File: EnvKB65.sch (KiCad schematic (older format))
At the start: 153 parts, among them U1 Pico

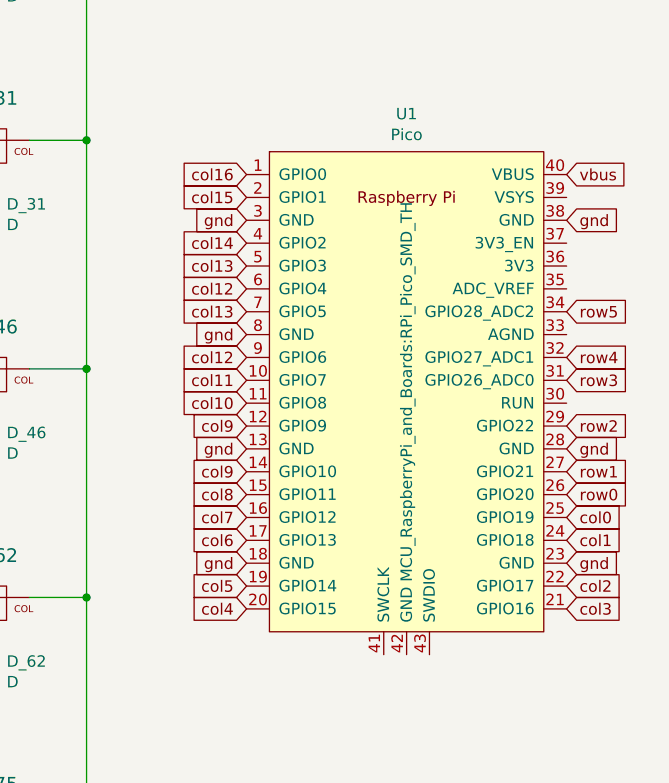
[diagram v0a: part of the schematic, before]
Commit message: slimmed design down a bit at the cost of some keys
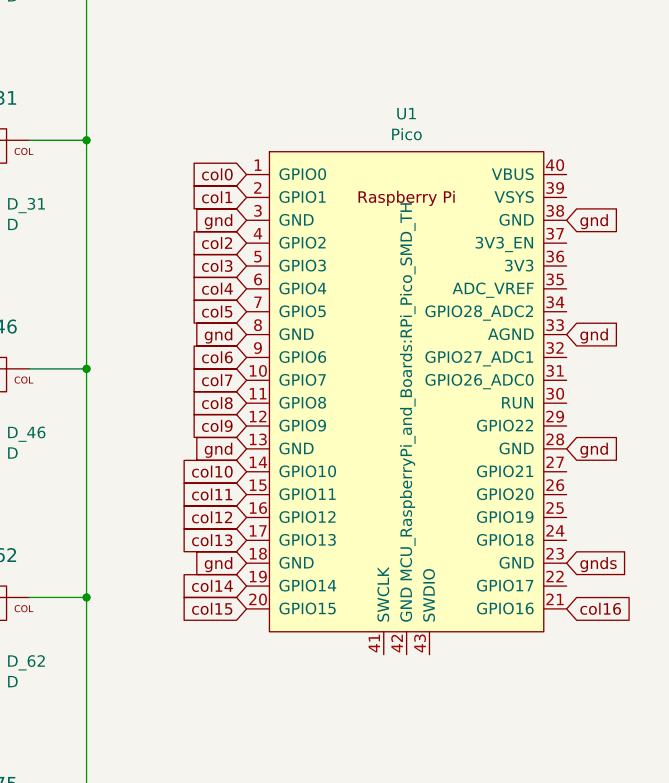
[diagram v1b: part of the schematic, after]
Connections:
- net col0: now also U1.1 (GPIO0); no longer U1.25 (GPIO19)
- net col1: now also U1.2 (GPIO1); no longer U1.24 (GPIO18)
- net col10: now also U1.14 (GPIO10); no longer U1.11 (GPIO8)
- net col11: now also U1.15 (GPIO11); no longer U1.10 (GPIO7)
- net col12: now also U1.16 (GPIO12); no longer U1.6 (GPIO4), U1.9 (GPIO6)
- net col13: now also U1.17 (GPIO13); no longer U1.5 (GPIO3), U1.7 (GPIO5)
- net col14: now also U1.19 (GPIO14); no longer U1.4 (GPIO2)
- net col15: now also U1.20 (GPIO15); no longer U1.2 (GPIO1)
- net col16: now also U1.21 (GPIO16); no longer U1.1 (GPIO0)
- net col2: now also U1.4 (GPIO2); no longer U1.22 (GPIO17)
- net col3: now also U1.5 (GPIO3); no longer U1.21 (GPIO16)
- net col4: now also U1.6 (GPIO4); no longer U1.20 (GPIO15)
- net col5: now also U1.7 (GPIO5); no longer U1.19 (GPIO14)
- net col6: now also U1.9 (GPIO6); no longer U1.17 (GPIO13)
- net col7: now also U1.10 (GPIO7); no longer U1.16 (GPIO12)
- net col8: now also U1.11 (GPIO8); no longer U1.15 (GPIO11)
- net col9: no longer U1.14 (GPIO10)
- net gnd: now also U1.33 (AGND); no longer U1.23 (GND)
- net row0: no longer U1.26 (GPIO20)
- net row1: no longer U1.27 (GPIO21)
- net row2: no longer U1.29 (GPIO22)
- net row3: no longer U1.31 (GPIO26_ADC0)
- net row4: no longer U1.32 (GPIO27_ADC1)
- net row5: no longer names the net of U1.34 (GPIO28_ADC2)
- net vbus: no longer names the net of U1.40 (VBUS)
- new net gnds: U1.23 (GND)
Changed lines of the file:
@@
 Wire Wire Line
 	17800 650  17800 950
-$Comp
-L MX_Alps_Hybrid:MX-NoLED K_15
-U 1 1 00000151
-P 17400 1000
-F 0 "K_15" H 17400 1233 60  0000 C CNN
-F 1 "KEYSW" H 17400 900 60  0001 C CNN
-F 2 "MX_Only:MXOnly-1U-NoLED" H 17400 1000 60  0001 C CNN
-F 3 "" H 17400 1000 60  0000 C CNN
-	1    17400 1000
-	1    0    0    -1
-$EndComp
-$Comp
-L Device:D_Small D_15
-U 1 1 00000150
-P 17350 1300
-F 0 "D_15" V 17420 1200 50  0000 R CNN
-F 1 "D" V 17330 1200 50  0000 R CNN
-F 2 "Diode_SMD:D_SOD-123" H 17050 1250 50  0001 C CNN
-F 3 "~" H 17050 1250 50  0001 C CNN
-	1    17350 1300
-	0    -1   -1   0
-$EndComp
 Wire Wire Line
 	17550 950  17800 950
-Wire Wire Line
-	17350 1150 17350 1200
 Connection ~ 17800 950
 Text GLabel 900  2400 0    50   Input ~ 0
@@
 Connection ~ 16800 1950
 Connection ~ 16350 2400
-$Comp
-L MX_Alps_Hybrid:MX-NoLED K_31
-U 1 1 00000311
-P 17400 2000
-F 0 "K_31" H 17400 2233 60  0000 C CNN
-F 1 "KEYSW" H 17400 1900 60  0001 C CNN
-F 2 "MX_Only:MXOnly-1U-NoLED" H 17400 2000 60  0001 C CNN
-F 3 "" H 17400 2000 60  0000 C CNN
-	1    17400 2000
-	1    0    0    -1
-$EndComp
-$Comp
-L Device:D_Small D_31
-U 1 1 00000310
-P 17350 2300
-F 0 "D_31" V 17420 2200 50  0000 R CNN
-F 1 "D" V 17330 2200 50  0000 R CNN
-F 2 "Diode_SMD:D_SOD-123" H 17050 2250 50  0001 C CNN
-F 3 "~" H 17050 2250 50  0001 C CNN
-	1    17350 2300
-	0    -1   -1   0
-$EndComp
 Wire Wire Line
 	17550 1950 17800 1950
-Wire Wire Line
-	17350 2150 17350 2200
 Connection ~ 17800 1950
 Text GLabel 900  3400 0    50   Input ~ 0
@@
 Connection ~ 16800 2950
 Connection ~ 16350 3400
-$Comp
-L MX_Alps_Hybrid:MX-NoLED K_46
-U 1 1 00000461
-P 17400 3000
-F 0 "K_46" H 17400 3233 60  0000 C CNN
-F 1 "KEYSW" H 17400 2900 60  0001 C CNN
-F 2 "MX_Only:MXOnly-1U-NoLED" H 17400 3000 60  0001 C CNN
-F 3 "" H 17400 3000 60  0000 C CNN
-	1    17400 3000
-	1    0    0    -1
-$EndComp
-$Comp
-L Device:D_Small D_46
-U 1 1 00000460
-P 17350 3300
-F 0 "D_46" V 17420 3200 50  0000 R CNN
-F 1 "D" V 17330 3200 50  0000 R CNN
-F 2 "Diode_SMD:D_SOD-123" H 17050 3250 50  0001 C CNN
-F 3 "~" H 17050 3250 50  0001 C CNN
-	1    17350 3300
-	0    -1   -1   0
-$EndComp
 Wire Wire Line
 	17550 2950 17800 2950
-Wire Wire Line
-	17350 3150 17350 3200
 Connection ~ 17800 2950
 Text GLabel 900  4400 0    50   Input ~ 0
@@
 	1    0    0    -1
 $EndComp
-Text GLabel 18500 2100 0    50   Input ~ 0
-col16
-Text GLabel 18500 2200 0    50   Input ~ 0
-col15
-Text GLabel 18500 2400 0    50   Input ~ 0
-col14
+$Comp
+L MX_Alps_Hybrid:MX-NoLED K_46
+U 1 1 60BC42E1
+P 17400 3000
+F 0 "K_46" H 17400 3233 60  0000 C CNN
+F 1 "KEYSW" H 17400 2900 60  0001 C CNN
+F 2 "MX_Only:MXOnly-1U-NoLED" H 17400 3000 60  0001 C CNN
+F 3 "" H 17400 3000 60  0000 C CNN
+	1    17400 3000
+	1    0    0    -1
+$EndComp
+$Comp
+L Device:D_Small D_46
+U 1 1 60BC42E7
+P 17350 3300
+F 0 "D_46" V 17420 3200 50  0000 R CNN
+F 1 "D" V 17330 3200 50  0000 R CNN
+F 2 "Diode_SMD:D_SOD-123" H 17050 3250 50  0001 C CNN
+F 3 "~" H 17050 3250 50  0001 C CNN
+	1    17350 3300
+	0    -1   -1   0
+$EndComp
+Wire Wire Line
+	17350 3150 17350 3200
+$Comp
+L MX_Alps_Hybrid:MX-NoLED K_31
+U 1 1 60BDC99E
+P 17400 2000
+F 0 "K_31" H 17400 2233 60  0000 C CNN
+F 1 "KEYSW" H 17400 1900 60  0001 C CNN
+F 2 "MX_Only:MXOnly-1U-NoLED" H 17400 2000 60  0001 C CNN
+F 3 "" H 17400 2000 60  0000 C CNN
+	1    17400 2000
+	1    0    0    -1
+$EndComp
+$Comp
+L Device:D_Small D_31
+U 1 1 60BDC9A4
+P 17350 2300
+F 0 "D_31" V 17420 2200 50  0000 R CNN
+F 1 "D" V 17330 2200 50  0000 R CNN
+F 2 "Diode_SMD:D_SOD-123" H 17050 2250 50  0001 C CNN
+F 3 "~" H 17050 2250 50  0001 C CNN
+	1    17350 2300
+	0    -1   -1   0
+$EndComp
+Wire Wire Line
+	17350 2150 17350 2200
+$Comp
+L MX_Alps_Hybrid:MX-NoLED K_15
+U 1 1 60C0E1CF
+P 17400 1000
+F 0 "K_15" H 17400 1233 60  0000 C CNN
+F 1 "KEYSW" H 17400 900 60  0001 C CNN
+F 2 "MX_Only:MXOnly-1U-NoLED" H 17400 1000 60  0001 C CNN
+F 3 "" H 17400 1000 60  0000 C CNN
+	1    17400 1000
+	1    0    0    -1
+$EndComp
+$Comp
+L Device:D_Small D_15
+U 1 1 60C0E1D5
+P 17350 1300
+F 0 "D_15" V 17420 1200 50  0000 R CNN
+F 1 "D" V 17330 1200 50  0000 R CNN
+F 2 "Diode_SMD:D_SOD-123" H 17050 1250 50  0001 C CNN
+F 3 "~" H 17050 1250 50  0001 C CNN
+	1    17350 1300
+	0    -1   -1   0
+$EndComp
+Wire Wire Line
+	17350 1150 17350 1200
 Text GLabel 18500 2300 0    50   Input ~ 0
-gnd
-Text GLabel 18500 2500 0    50   Input ~ 0
-col13
-Text GLabel 18500 2600 0    50   Input ~ 0
-col12
-Text GLabel 18500 2700 0    50   Input ~ 0
-col13
-Text GLabel 18500 2900 0    50   Input ~ 0
-col12
-Text GLabel 18500 3000 0    50   Input ~ 0
-col11
-Text GLabel 18500 3100 0    50   Input ~ 0
-col10
-Text GLabel 18500 3200 0    50   Input ~ 0
-col9
-Text GLabel 18500 3300 0    50   Input ~ 0
 gnd
 Text GLabel 18500 2800 0    50   Input ~ 0
 gnd
-Text GLabel 18500 3400 0    50   Input ~ 0
-col9
-Text GLabel 18500 3500 0    50   Input ~ 0
-col8
-Text GLabel 18500 3600 0    50   Input ~ 0
-col7
-Text GLabel 18500 3700 0    50   Input ~ 0
-col6
+Text GLabel 18500 3300 0    50   Input ~ 0
+gnd
 Text GLabel 18500 3800 0    50   Input ~ 0
 gnd
-Text GLabel 18500 3900 0    50   Input ~ 0
-col5
-Text GLabel 18500 4000 0    50   Input ~ 0
-col4
-Text GLabel 19900 4000 2    50   Input ~ 0
-col3
-Text GLabel 19900 3900 2    50   Input ~ 0
-col2
 Text GLabel 19900 3800 2    50   Input ~ 0
-gnd
-Text GLabel 19900 3700 2    50   Input ~ 0
-col1
-Text GLabel 19900 3600 2    50   Input ~ 0
-col0
-Text GLabel 19900 3500 2    50   Input ~ 0
-row0
-Text GLabel 19900 3400 2    50   Input ~ 0
-row1
+gnds
 Text GLabel 19900 3300 2    50   Input ~ 0
 gnd
-Text GLabel 19900 3200 2    50   Input ~ 0
-row2
-Text GLabel 19900 3000 2    50   Input ~ 0
-row3
-Text GLabel 19900 2900 2    50   Input ~ 0
-row4
-Text GLabel 19900 2700 2    50   Input ~ 0
-row5
-Text GLabel 19900 2100 2    50   Input ~ 0
-vbus
 Text GLabel 19900 2300 2    50   Input ~ 0
 gnd
+Text GLabel 19900 2800 2    50   Input ~ 0
+gnd
+Text GLabel 18500 2100 0    50   Input ~ 0
+col0
+Text GLabel 18500 2200 0    50   Input ~ 0
+col1
+Text GLabel 18500 2400 0    50   Input ~ 0
+col2
+Text GLabel 18500 2500 0    50   Input ~ 0
+col3
+Text GLabel 18500 2600 0    50   Input ~ 0
+col4
+Text GLabel 18500 2700 0    50   Input ~ 0
+col5
+Text GLabel 18500 2900 0    50   Input ~ 0
+col6
+Text GLabel 18500 3000 0    50   Input ~ 0
+col7
+Text GLabel 18500 3100 0    50   Input ~ 0
+col8
+Text GLabel 18500 3200 0    50   Input ~ 0
+col9
+Text GLabel 18500 3400 0    50   Input ~ 0
+col10
+Text GLabel 18500 3500 0    50   Input ~ 0
+col11
+Text GLabel 18500 3600 0    50   Input ~ 0
+col12
+Text GLabel 18500 3700 0    50   Input ~ 0
+col13
+Text GLabel 18500 3900 0    50   Input ~ 0
+col14
+Text GLabel 18500 4000 0    50   Input ~ 0
+col15
+Text GLabel 19900 4000 2    50   Input ~ 0
+col16
 $EndSCHEMATC

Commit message: Routed Traces, Add Mounting holes and edge cuts
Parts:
- added H1, H2, H3, H4, H5, H6: MountingHole, MountingHole:MountingHole_2.2mm_M2, symbol Mechanical:MountingHole
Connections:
- net gnds is gone; now on net gnd: U1.23 (GND)
- net row0: now also U1.27 (GPIO21)
- net row1: now also U1.26 (GPIO20)
- net row2: now also U1.25 (GPIO19)
- net row3: now also U1.24 (GPIO18)
- net row4: now also U1.22 (GPIO17)
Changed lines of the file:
@@
 gnd
 Text GLabel 19900 3800 2    50   Input ~ 0
-gnds
+gnd
 Text GLabel 19900 3300 2    50   Input ~ 0
 gnd
@@
 Text GLabel 19900 4000 2    50   Input ~ 0
 col16
+Text GLabel 19900 3900 2    50   Input ~ 0
+row4
+Text GLabel 19900 3700 2    50   Input ~ 0
+row3
+Text GLabel 19900 3600 2    50   Input ~ 0
+row2
+Text GLabel 19900 3500 2    50   Input ~ 0
+row1
+Text GLabel 19900 3400 2    50   Input ~ 0
+row0
+$Comp
+L Mechanical:MountingHole H1
+U 1 1 60AC66FB
+P 4850 6150
+F 0 "H1" H 4950 6196 50  0000 L CNN
+F 1 "MountingHole" H 4950 6105 50  0000 L CNN
+F 2 "MountingHole:MountingHole_2.2mm_M2" H 4850 6150 50  0001 C CNN
+F 3 "~" H 4850 6150 50  0001 C CNN
+	1    4850 6150
+	1    0    0    -1
+$EndComp
+$Comp
+L Mechanical:MountingHole H2
+U 1 1 60ACBE92
+P 4850 6350
+F 0 "H2" H 4950 6396 50  0000 L CNN
+F 1 "MountingHole" H 4950 6305 50  0000 L CNN
+F 2 "MountingHole:MountingHole_2.2mm_M2" H 4850 6350 50  0001 C CNN
+F 3 "~" H 4850 6350 50  0001 C CNN
+	1    4850 6350
+	1    0    0    -1
+$EndComp
+$Comp
+L Mechanical:MountingHole H3
+U 1 1 60AE412B
+P 4850 6550
+F 0 "H3" H 4950 6596 50  0000 L CNN
+F 1 "MountingHole" H 4950 6505 50  0000 L CNN
+F 2 "MountingHole:MountingHole_2.2mm_M2" H 4850 6550 50  0001 C CNN
+F 3 "~" H 4850 6550 50  0001 C CNN
+	1    4850 6550
+	1    0    0    -1
+$EndComp
+$Comp
+L Mechanical:MountingHole H4
+U 1 1 60AFC1C3
+P 4850 6750
+F 0 "H4" H 4950 6796 50  0000 L CNN
+F 1 "MountingHole" H 4950 6705 50  0000 L CNN
+F 2 "MountingHole:MountingHole_2.2mm_M2" H 4850 6750 50  0001 C CNN
+F 3 "~" H 4850 6750 50  0001 C CNN
+	1    4850 6750
+	1    0    0    -1
+$EndComp
+$Comp
+L Mechanical:MountingHole H5
+U 1 1 60B142B5
+P 4850 6950
+F 0 "H5" H 4950 6996 50  0000 L CNN
+F 1 "MountingHole" H 4950 6905 50  0000 L CNN
+F 2 "MountingHole:MountingHole_2.2mm_M2" H 4850 6950 50  0001 C CNN
+F 3 "~" H 4850 6950 50  0001 C CNN
+	1    4850 6950
+	1    0    0    -1
+$EndComp
+$Comp
+L Mechanical:MountingHole H6
+U 1 1 60B2C4B8
+P 4850 7150
+F 0 "H6" H 4950 7196 50  0000 L CNN
+F 1 "MountingHole" H 4950 7105 50  0000 L CNN
+F 2 "MountingHole:MountingHole_2.2mm_M2" H 4850 7150 50  0001 C CNN
+F 3 "~" H 4850 7150 50  0001 C CNN
+	1    4850 7150
+	1    0    0    -1
+$EndComp
 $EndSCHEMATC

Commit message: Changed Diodes to SOD-323 and separated Position files
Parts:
- D_0, D_1, D_10, D_11, D_12, D_13, D_14, D_15, D_16, D_17, D_18, D_19, D_2, D_20, D_21, D_22, D_23, D_24, D_25, D_26, D_27, D_28, D_29, D_3, D_30, D_31, D_32, D_33, D_34, D_35, D_36, D_37, D_38, D_39, D_4, D_40, D_41, D_42, D_43, D_44, D_45, D_46, D_47, D_48, D_49, D_5, D_50, D_51, D_52, D_53, D_54, D_55, D_56, D_57, D_58, D_59, D_6, D_60, D_61, D_62, D_63, D_64, D_65, D_66, D_67, D_68, D_69, D_7, D_70, D_71, D_72, D_73, D_74, D_75, D_8, D_9: value D -> Diode SOD-323; footprint Diode_SMD:D_SOD-123 -> Diode_SMD:D_SOD-323_HandSoldering
